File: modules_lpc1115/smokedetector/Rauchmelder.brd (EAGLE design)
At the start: 38 x 65 mm, 75 parts, among them IC1 BD9G101, IC2 LPC1115, Q1 BC856, Q3 BCP52, Q4 ASFL, T1 BC847C, T2 BC817

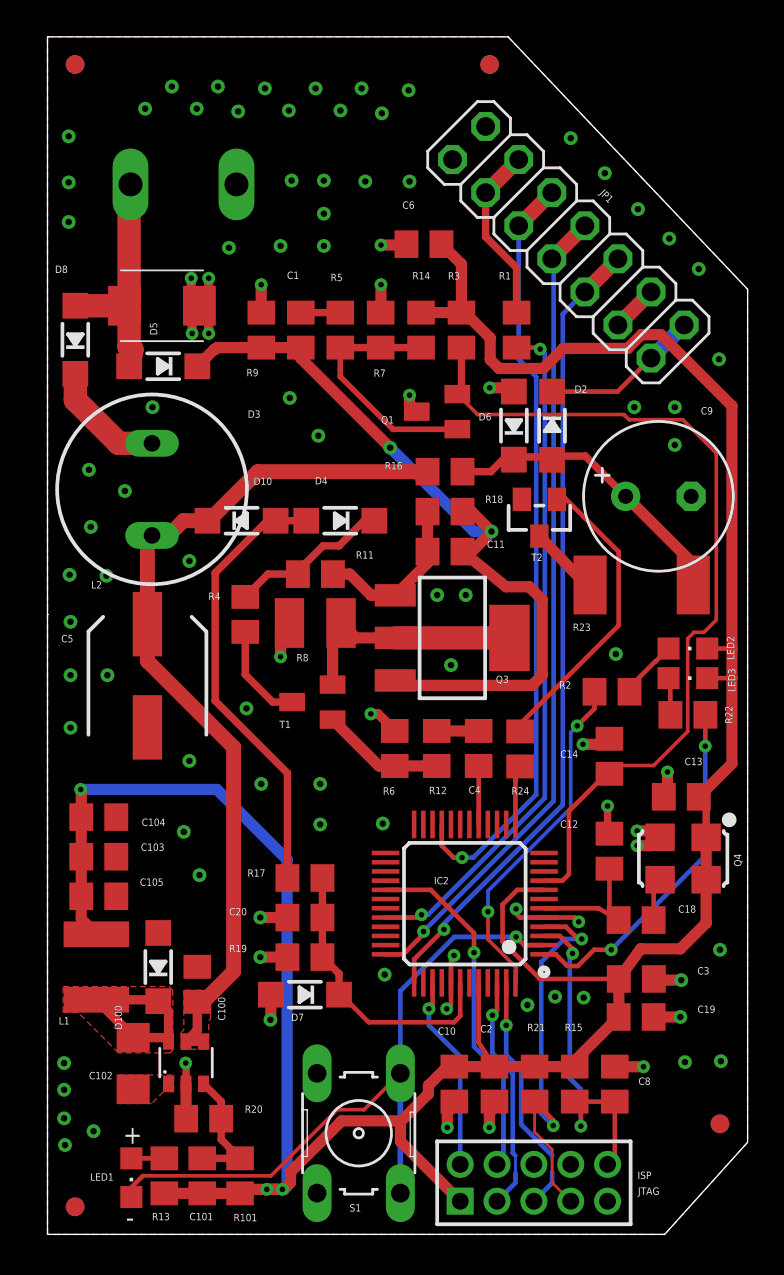
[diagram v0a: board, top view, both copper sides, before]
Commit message: [RM] - rearranged diodes; added holes for pull out zip tie
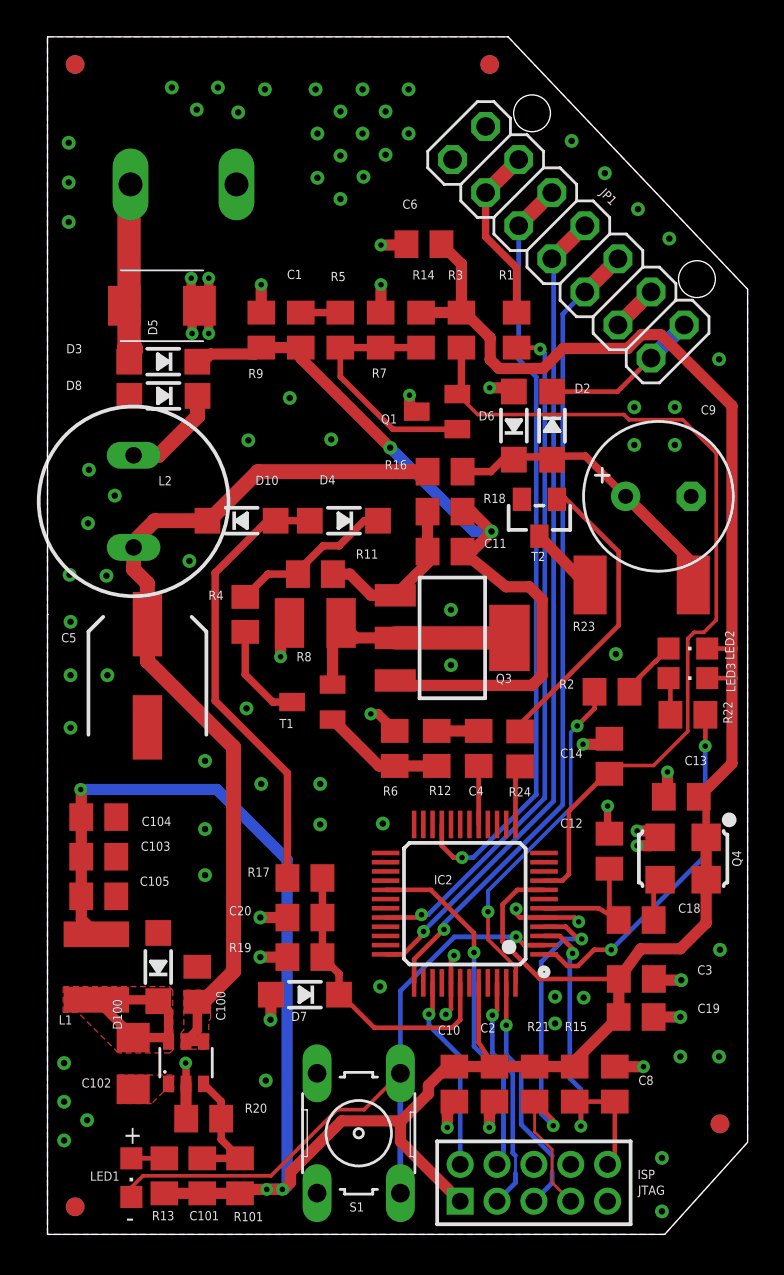
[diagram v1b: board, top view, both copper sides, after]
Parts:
- C20: value 100n -> 100nF
- R8: value 5R6 -> 5R6 1210
- moved D8 5.67 mm to (6.29, 45.5), turned to 180 degrees
- moved L2 1.19 mm to (4.67, 39.8)
- moved D3 0.25 mm to (6.28, 47.4)
- moved D4 0.20 mm to (16.1, 38.7)
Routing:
- net EIB+: track 12.9 -> 9.92 mm
- net N$13: track 6.55 -> 5.46 mm
- net EIB_DC: track 48.1 -> 49.1 mm
- net GND: track 49.0 -> 49.3 mm, vias 98 -> 97
